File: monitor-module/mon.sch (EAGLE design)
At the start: 11 parts

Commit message: submitted
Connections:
- new net N$3: U$1.PA0, U$2.DIO0
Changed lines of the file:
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@@
 <?xml version="1.0" encoding="utf-8"?>
 <!DOCTYPE eagle SYSTEM "eagle.dtd">
-<eagle version="6.5.0">
+<eagle version="6.6.0">
 <drawing>
 <settings>
@@
 <pinref part="DISP" gate="G$1" pin="5"/>
 <wire x1="22.86" y1="48.26" x2="25.4" y2="48.26" width="0.1524" layer="91"/>
+<label x="25.4" y="48.26" size="1.27" layer="95" font="vector" xref="yes"/>
 </segment>
 </net>
@@
 <pinref part="DISP" gate="G$1" pin="3"/>
 <wire x1="22.86" y1="43.18" x2="25.4" y2="43.18" width="0.1524" layer="91"/>
+<label x="25.4" y="43.18" size="1.27" layer="95" font="vector" xref="yes"/>
 </segment>
 </net>
@@
 <pinref part="DISP" gate="G$1" pin="4"/>
 <wire x1="22.86" y1="45.72" x2="25.4" y2="45.72" width="0.1524" layer="91"/>
+<label x="25.4" y="45.72" size="1.27" layer="95" font="vector" xref="yes"/>
 </segment>
 </net>
@@
 <pinref part="DISP" gate="G$1" pin="6"/>
 <wire x1="22.86" y1="50.8" x2="25.4" y2="50.8" width="0.1524" layer="91"/>
-</segment>
-</net>
+<label x="25.4" y="50.8" size="1.27" layer="95" font="vector" xref="yes"/>
+</segment>
+</net>
+<net name="N$3" class="0">
+<segment>
+<pinref part="U$1" gate="G$1" pin="PA0"/>
+<wire x1="121.92" y1="134.62" x2="152.4" y2="134.62" width="0.1524" layer="91"/>
+<wire x1="152.4" y1="134.62" x2="152.4" y2="109.22" width="0.1524" layer="91"/>
+<wire x1="152.4" y1="109.22" x2="218.44" y2="109.22" width="0.1524" layer="91"/>
+<wire x1="218.44" y1="109.22" x2="218.44" y2="121.92" width="0.1524" layer="91"/>
+<pinref part="U$2" gate="A" pin="DIO0"/>
+<wire x1="218.44" y1="121.92" x2="208.28" y2="121.92" width="0.1524" layer="91"/>
+</segment>
+</net>

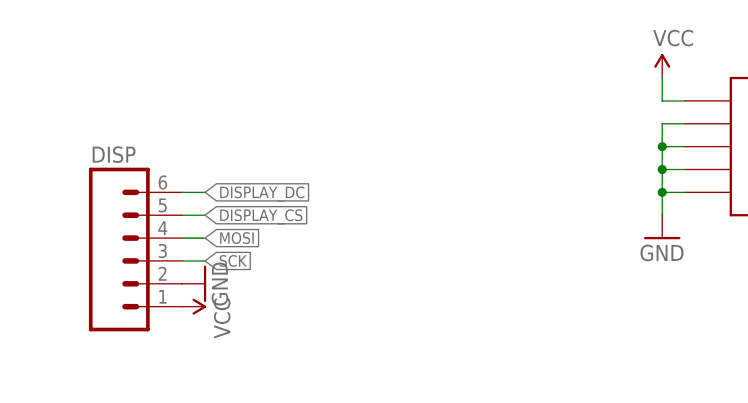
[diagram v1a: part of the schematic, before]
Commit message: added jumpers because dont trust ebay sellers
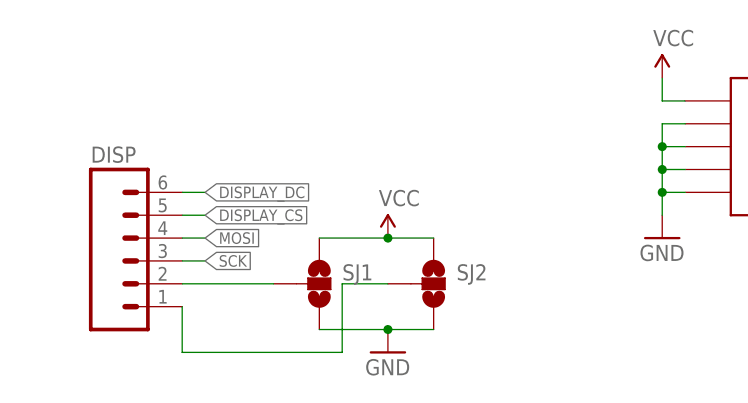
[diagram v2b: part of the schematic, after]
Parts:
- added SJ1, SJ2: (no value), SparkFun-Retired:SOLDERJUMPER_2WAYS
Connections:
- new net N$4: DISP.2, SJ1.2
- new net N$5: DISP.1, SJ2.2
- net GND: now also SJ1.3, SJ2.3; no longer DISP.2
- net VCC: now also SJ1.1, SJ2.1; no longer DISP.1
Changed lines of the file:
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@@
 <part name="GND17" library="SparkFun-Aesthetics" deviceset="GND" device=""/>
 <part name="DISP" library="SparkFun-Connectors" deviceset="M06" device="SILK_FEMALE_PTH"/>
-<part name="SUPPLY7" library="SparkFun-Aesthetics" deviceset="VCC" device=""/>
 <part name="GND18" library="SparkFun-Aesthetics" deviceset="GND" device=""/>
+<part name="SJ1" library="SparkFun-Retired" deviceset="SOLDERJUMPER_2WAY" device="S"/>
+<part name="SJ2" library="SparkFun-Retired" deviceset="SOLDERJUMPER_2WAY" device="S"/>
+<part name="SUPPLY6" library="SparkFun-Aesthetics" deviceset="VCC" device=""/>
 </parts>
 <sheets>
@@
 <instance part="GND17" gate="1" x="162.56" y="154.94" rot="R90"/>
 <instance part="DISP" gate="G$1" x="17.78" y="43.18"/>
-<instance part="SUPPLY7" gate="G$1" x="22.86" y="38.1" rot="R270"/>
-<instance part="GND18" gate="1" x="25.4" y="40.64" rot="R90"/>
+<instance part="GND18" gate="1" x="45.72" y="33.02"/>
+<instance part="SJ1" gate="G$1" x="38.1" y="40.64"/>
+<instance part="SJ2" gate="G$1" x="50.8" y="40.64"/>
+<instance part="SUPPLY6" gate="G$1" x="45.72" y="45.72"/>
 </instances>
 <busses>
@@
 </segment>
 <segment>
-<pinref part="DISP" gate="G$1" pin="2"/>
+<pinref part="SJ2" gate="G$1" pin="3"/>
 <pinref part="GND18" gate="1" pin="GND"/>
+<wire x1="50.8" y1="35.56" x2="45.72" y2="35.56" width="0.1524" layer="91"/>
+<pinref part="SJ1" gate="G$1" pin="3"/>
+<wire x1="38.1" y1="35.56" x2="45.72" y2="35.56" width="0.1524" layer="91"/>
+<junction x="45.72" y="35.56"/>
 </segment>
 </net>
@@
 </segment>
 <segment>
-<pinref part="DISP" gate="G$1" pin="1"/>
-<pinref part="SUPPLY7" gate="G$1" pin="VCC"/>
+<pinref part="SUPPLY6" gate="G$1" pin="VCC"/>
+<pinref part="SJ2" gate="G$1" pin="1"/>
+<wire x1="45.72" y1="45.72" x2="50.8" y2="45.72" width="0.1524" layer="91"/>
+<pinref part="SJ1" gate="G$1" pin="1"/>
+<wire x1="45.72" y1="45.72" x2="38.1" y2="45.72" width="0.1524" layer="91"/>
+<junction x="45.72" y="45.72"/>
 </segment>
 </net>
@@
 </segment>
 </net>
+<net name="N$4" class="0">
+<segment>
+<pinref part="SJ1" gate="G$1" pin="2"/>
+<pinref part="DISP" gate="G$1" pin="2"/>
+<wire x1="33.02" y1="40.64" x2="22.86" y2="40.64" width="0.1524" layer="91"/>
+</segment>
+</net>
+<net name="N$5" class="0">
+<segment>
+<pinref part="SJ2" gate="G$1" pin="2"/>
+<wire x1="45.72" y1="40.64" x2="40.64" y2="40.64" width="0.1524" layer="91"/>
+<wire x1="40.64" y1="40.64" x2="40.64" y2="33.02" width="0.1524" layer="91"/>
+<wire x1="40.64" y1="33.02" x2="22.86" y2="33.02" width="0.1524" layer="91"/>
+<pinref part="DISP" gate="G$1" pin="1"/>
+<wire x1="22.86" y1="33.02" x2="22.86" y2="38.1" width="0.1524" layer="91"/>
+</segment>
+</net>
